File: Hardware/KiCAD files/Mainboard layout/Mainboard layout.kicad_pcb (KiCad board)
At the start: 2 copper layers, 125.7 x 122.4 mm, 62 parts, among them J1 Programmer pins Conn_01x02, J10 Conn_01x02, J11 Conn_01x06, J12 JST_06, J13 Conn_01x08, J14 Conn_01x03, J15 Conn_01x03, J17 Conn_01x06, J19 Conn_01x06, J2 Screw_Terminal_2_P5.00mm, J21 Conn_01x06, J22 Conn_01x03, J23 Conn_01x06, J24 Conn_01x06, J25 Conn_01x06, J26 Conn_01x06, J28 Conn_01x03, J29 Conn_01x03, J3 Screw_Terminal_2_P3.50mm, J30 USB-A1VSB6, J31 JST_03, J34 JST_03, J35 JST_03, J36 JST_03, J37 JST_03, J38 JST_03, J4 JST_06, J5 Conn_01x04, J6 JST_06, J7 JST_06, J8 Conn_01x06, J9 Conn_01x10, Q2 2DD1664, Q5 2N7000, SW8 Push_Button, SW9 Push_Button, U12 ESP32-S3-WROOM-1, U3 PCA9534PW, U5 PCA9534PW

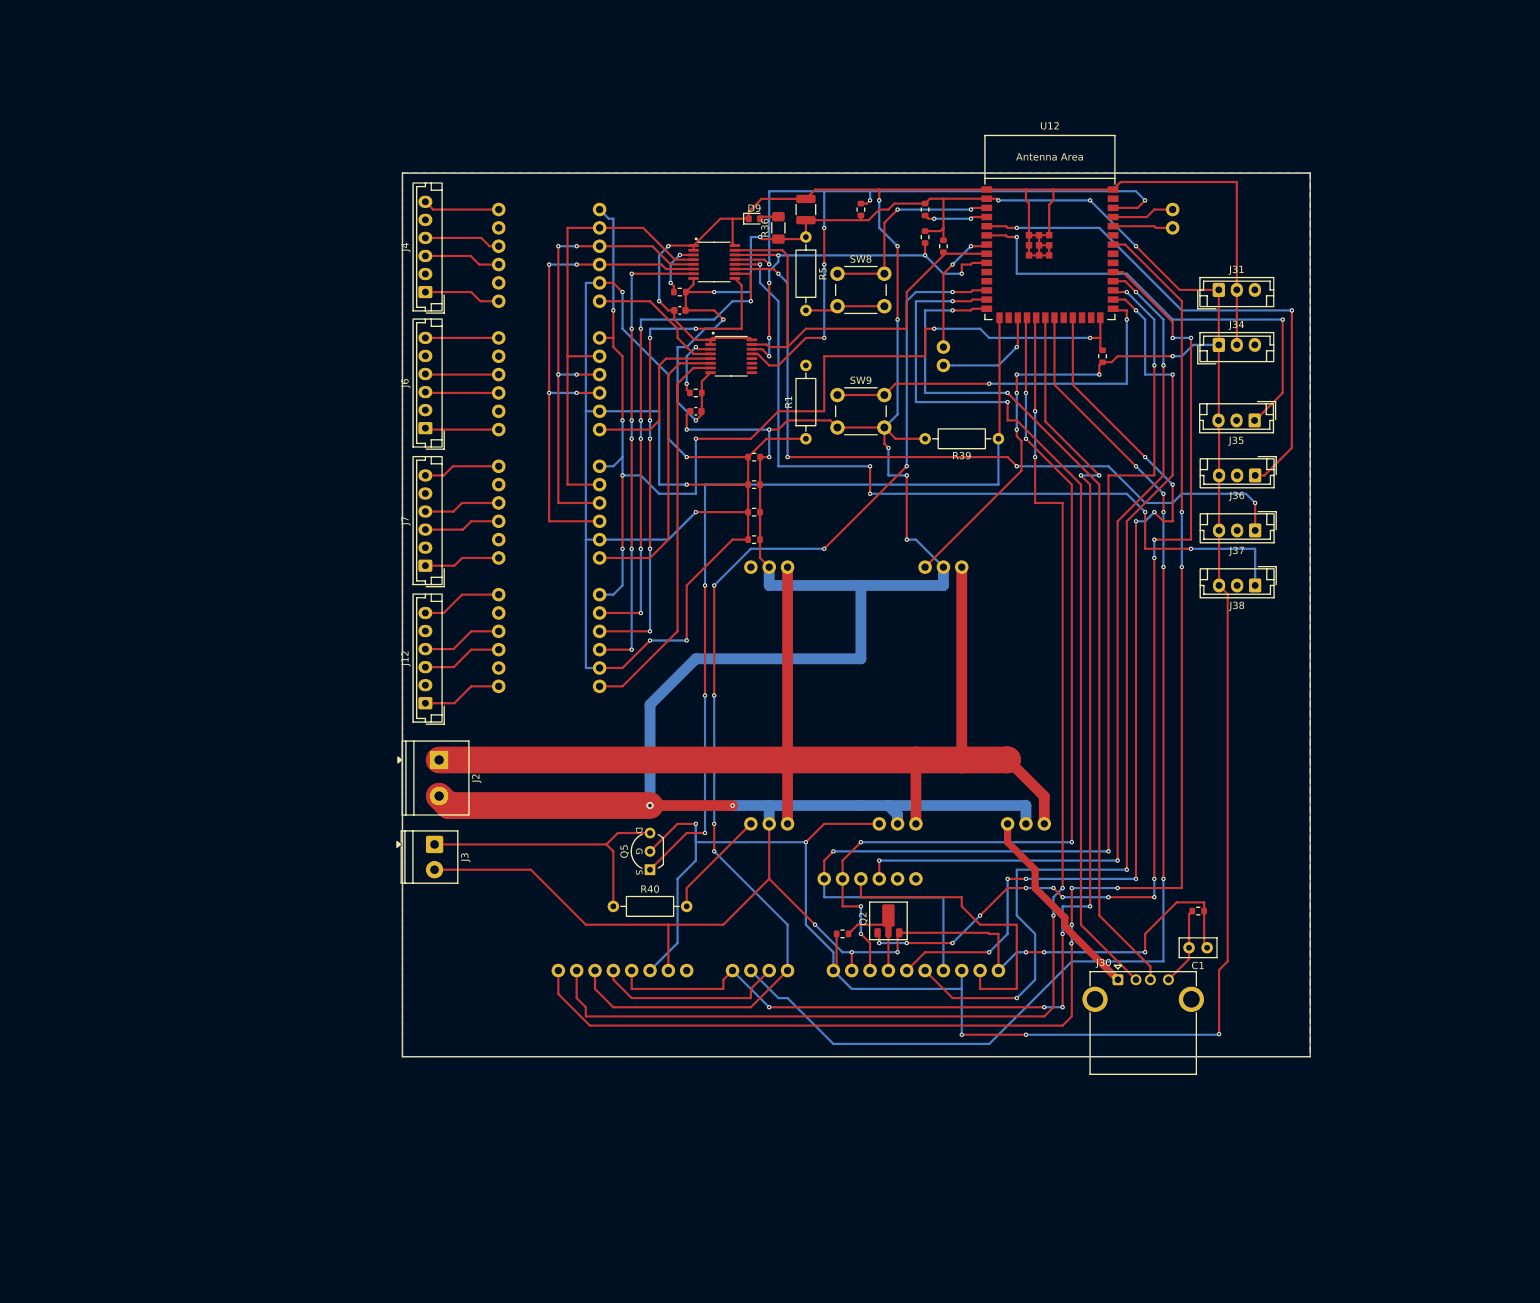
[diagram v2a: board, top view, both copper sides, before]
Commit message: 1st push of PCB's for printing
This is pre-peer review. This almost certainly has section that need adjustment. also realized I'm missing the USB-Uart bridge. first thing added in next version.
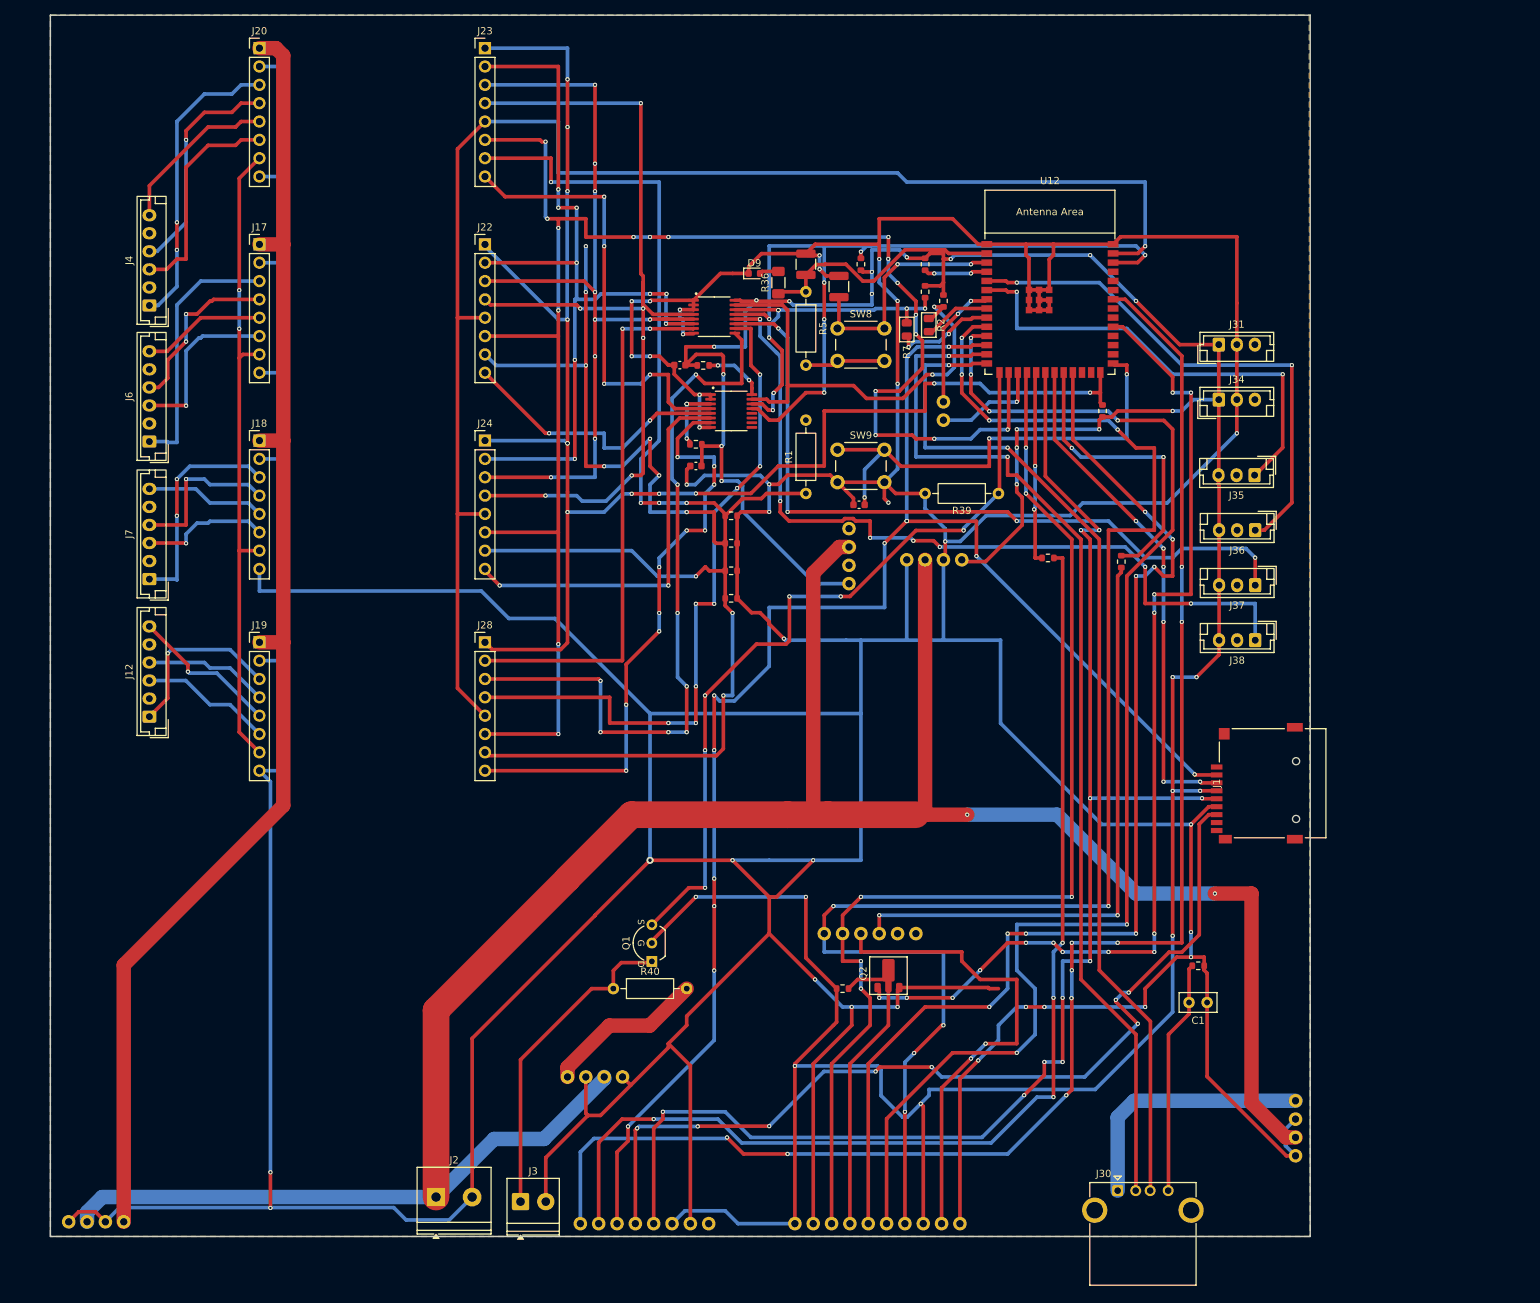
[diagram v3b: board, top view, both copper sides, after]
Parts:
- removed J14, J15, J29: Conn_01x03, PCM_SparkFun-Connector:1x03_P2.54mm
- removed J21: Conn_01x06, PCM_SparkFun-Connector:1x06_P2.54mm
- removed Q5: 2N7000, PCM_Package_TO_SOT_THT_AKL:TO-92_Inline_Wide_SGD
- removed R51: 10k, PCM_SparkFun-Resistor:R_0603_1608Metric
- added C3: 0.1uF, PCM_SparkFun-Capacitor:C_0603_1608Metric, F.Cu at (147.1, 59.9)
- added C4: 10uF, PCM_SparkFun-Capacitor:C_1210_3225Metric, F.Cu at (144.3, 29.7)
- added J18: PINHD_1x8_Male, Connector_PinHeader_2.54mm:PinHeader_1x08_P2.54mm_Vertical, F.Cu at (64.0, 51.1)
- added J20: PINHD_1x8_Male, Connector_PinHeader_2.54mm:PinHeader_1x08_P2.54mm_Vertical, F.Cu at (64.0, -3.30)
- added J27: Conn_01x04, PCM_SparkFun-Connector:1x04_P2.54mm, F.Cu at (106.7, 139.2)
- added Q1: BS170, PCM_Package_TO_SOT_THT_AKL:TO-92_Inline_Wide_DGS, F.Cu at (118.4, 123.2)
- added R2: 50 ohmR_0805, PCM_Resistor_SMD_AKL:R_0805_2012Metric, F.Cu at (156.7, 35.1)
- added R3: 100, PCM_SparkFun-Resistor:R_0603_1608Metric, F.Cu at (183.4, 67.8)
- added R4: 100, PCM_SparkFun-Resistor:R_0603_1608Metric, F.Cu at (173.2, 67.3)
- added R56: 10k, PCM_SparkFun-Resistor:R_0603_1608Metric, F.Cu at (124.5, 51.6)
- added R7: 50 ohm R_0805, PCM_Resistor_SMD_AKL:R_0805_2012Metric, F.Cu at (153.7, 35.7)
- J1: value Programmer pins Conn_01x02 -> MSD-1-A; footprint PCM_SparkFun-Connector:1x02_P2.54mm -> MMC_Footprints:CONN9_MSD-1_CUD
- J11, J25, J26: value Conn_01x06 -> Conn_01x04; footprint PCM_SparkFun-Connector:1x06_P2.54mm -> PCM_SparkFun-Connector:1x04_P2.54mm
- J17, J19, J23, J24: value Conn_01x06 -> PINHD_1x8_Male; footprint PCM_SparkFun-Connector:1x06_P2.54mm -> Connector_PinHeader_2.54mm:PinHeader_1x08_P2.54mm_Vertical
- J22, J28: value Conn_01x03 -> PINHD_1x8_Male; footprint PCM_SparkFun-Connector:1x03_P2.54mm -> Connector_PinHeader_2.54mm:PinHeader_1x08_P2.54mm_Vertical
- R50: value 10k -> 1k
- moved J11 137.7 mm to (45.2, 159.3), turned to 180 degrees
- moved J25 122.2 mm to (207.5, 142.5), turned to -90 degrees
- moved J1 80.7 mm to (204.3, 98.5), turned to 90 degrees
- moved J28 76.6 mm to (95.2, 79.0)
- moved J22 75.6 mm to (95.2, 23.9)
- moved J5 61.8 mm to (161.3, 67.6)
- moved J2 60.5 mm to (88.5, 155.8), turned to 0 degrees
- moved J3 50.9 mm to (100.2, 156.5), turned to 0 degrees
- moved J17 41.9 mm to (64.0, 23.9), turned to 0 degrees
- moved J23 38.5 mm to (95.2, -3.30), turned to 0 degrees
- moved J12 38.3 mm to (48.8, 89.3)
- moved J4 38.3 mm to (48.8, 32.3)
- moved J6 38.3 mm to (48.8, 51.2)
- moved J7 38.3 mm to (48.8, 70.2)
- moved J26 37.4 mm to (145.7, 70.9)
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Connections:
- J1 pad 1: /TX -> unconnected-(J1-DAT2-Pad1)
- J1 pad 2: /RX -> SPI1_CS
- J11 pad 1: B2_DRV0 -> +12V
- J11 pad 2: unconnected-(J11-Pin_2-Pad2) -> GND
- J11 pad 3: A2_DRV0 -> +24V
- J11 pad 4: B1_DRV0 -> GND
- J12 pad 1: B2_DRV3 -> B2_DRVE
- J12 pad 3: A2_DRV3 -> A2_DRVE
- J12 pad 4: B1_DRV3 -> B1_DRVE
- J12 pad 6: A1_DRV3 -> A1_DRVE
- J17 pad 1: B2_DRV1 -> +12V
- J17 pad 2: unconnected-(J17-Pin_2-Pad2) -> GND
- J17 pad 3: A2_DRV1 -> B2_DRV1
- J17 pad 5: unconnected-(J17-Pin_5-Pad5) -> A1_DRV1
- J17 pad 6: A1_DRV1 -> A2_DRV1
- J19 pad 1: B2_DRV2 -> +12V
- J19 pad 2: unconnected-(J19-Pin_2-Pad2) -> GND
- J19 pad 3: A2_DRV2 -> B2_DRVE
- J19 pad 4: B1_DRV2 -> B1_DRVE
- J19 pad 5: unconnected-(J19-Pin_5-Pad5) -> A1_DRVE
- J19 pad 6: A1_DRV2 -> A2_DRVE
- J22 pad 1: +3.3V -> N_ENBL
- J22 pad 2: GND -> MODE_2_GPIO
- J22 pad 3: +24V -> MODE_1_GPIO
- J23 pad 1: DIR0 -> N_ENBL
- J23 pad 2: DRIVER_0_STEP -> MODE_2_GPIO
- J23 pad 3: MODE_2_GPIO -> MODE_1_GPIO
- J23 pad 4: MODE_1_GPIO -> MODE_0_GPIO
- J23 pad 5: MODE_0_GPIO -> Reset
- J23 pad 6: N_ENBL -> nSLP
- J24 pad 1: DIR1 -> N_ENBL
- J24 pad 2: DRIVER_0_STEP -> MODE_2_GPIO
- J24 pad 3: MODE_2_GPIO -> MODE_1_GPIO
- J24 pad 4: MODE_1_GPIO -> MODE_0_GPIO
- J24 pad 5: MODE_0_GPIO -> Reset
- J24 pad 6: N_ENBL -> nSLP
- J25 pad 1: DIR2 -> +5V_HIGHPW
- J25 pad 2: DRIVER_0_STEP -> GND
- J25 pad 3: MODE_2_GPIO -> +24V
- J25 pad 4: MODE_1_GPIO -> GND
- J26 pad 1: DIR3 -> +3.3V
- J26 pad 2: DRIVER_0_STEP -> GND
- J26 pad 3: MODE_2_GPIOE -> +24V
- J26 pad 4: MODE_1_GPIOE -> GND
- J28 pad 1: +5V_HIGHPW -> N_ENBL
- J28 pad 2: GND -> MODE_2_GPIOE
- J28 pad 3: +24V -> MODE_1_GPIOE
- J5 pad 1: SPI1_CS -> +3.3V
- J5 pad 2: CHAINL0_MISO_1 -> GND
- J5 pad 3: MOSI_1 -> +24V
- J5 pad 4: SPI1_CLK -> GND
- R52 pad 1: Net-(U12-GPIO16/U0CTS/ADC2_CH5/XTAL_32K_N) -> Net-(U3-SCL)
- R53 pad 1: Net-(U12-GPIO15/U0RTS/ADC2_CH4/XTAL_32K_P) -> Net-(U3-SDA)
- R54 pad 1: +3.3V -> Net-(U5-VDD)
- R54 pad 2: Net-(U5-A2) -> +3.3V
- U12 pad 10: unconnected-(U12-GPIO17/U1TXD/ADC2_CH6-Pad10) -> SPI4_CLK
- U12 pad 11: unconnected-(U12-GPIO18/U1RXD/ADC2_CH7/CLK_OUT3-Pad11) -> MOSI_4
- U12 pad 16: unconnected-(U12-GPIO46-Pad16) -> nSLP
- U12 pad 19: MISO_1 -> Net-(U12-GPIO11/TOUCH11/ADC2_CH0/FSPID/FSPIIO5/SUBSPID)
- U12 pad 22: unconnected-(U12-GPIO14/TOUCH14/ADC2_CH3/FSPIWP/FSPIDQS/SUBSPIWP-Pad22) -> Net-(U12-GPIO14/TOUCH14/ADC2_CH3/FSPIWP/FSPIDQS/SUBSPIWP)
- U12 pad 28: MOSI_4 -> unconnected-(U12-SPIIO6/GPIO35/FSPID/SUBSPID-Pad28)
- U12 pad 29: SPI4_CLK -> unconnected-(U12-SPIIO7/GPIO36/FSPICLK/SUBSPICLK-Pad29)
- U12 pad 30: MISO_4 -> unconnected-(U12-SPIDQS/GPIO37/FSPIQ/SUBSPIQ-Pad30)
- U12 pad 39: unconnected-(U12-GPIO1/TOUCH1/ADC1_CH0-Pad39) -> Reset
- U3 pad 14: Net-(U12-GPIO16/U0CTS/ADC2_CH5/XTAL_32K_N) -> Net-(U3-SCL)
- U3 pad 15: Net-(U12-GPIO15/U0RTS/ADC2_CH4/XTAL_32K_P) -> Net-(U3-SDA)
- U3 pad 16: GND -> +3.3V
- U3 pad 3: Net-(U3-A2) -> GND
- U3 pad 8: +3.3V -> GND
- U5 pad 14: Net-(U12-GPIO16/U0CTS/ADC2_CH5/XTAL_32K_N) -> Net-(U3-SCL)
- U5 pad 15: Net-(U12-GPIO15/U0RTS/ADC2_CH4/XTAL_32K_P) -> Net-(U3-SDA)
- U5 pad 16: GND -> Net-(U5-VDD)
- U5 pad 7: DIR3 -> DIRE
- U5 pad 8: +3.3V -> GND
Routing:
- net GND: track 607.6 -> 1227.7 mm, vias 19 -> 35
- net nSLP: track 0.00 -> 231.9 mm, vias 0 -> 18
- net Reset: track 0.00 -> 205.9 mm, vias 0 -> 1
- net +24V: track 160.9 -> 347.8 mm, vias 0 -> 2
- net +12V: track 0.00 -> 184.3 mm
- net CHAINL0_MISO_1: track 26.2 -> 127.9 mm, vias 0 -> 8
- net MOSI_1: track 161.5 -> 70.4 mm, vias 5 -> 6
- net nFault: track 0.00 -> 90.4 mm, vias 0 -> 2
- net DIRE: track 0.00 -> 82.7 mm, vias 0 -> 10
- net +3.3V: track 452.2 -> 530.3 mm, vias 17 -> 26
- net DRIVER_0_STEP: track 205.5 -> 282.4 mm, vias 6 -> 14
- net N_ENBL: track 156.1 -> 226.6 mm, vias 7 -> 12
- net MODE_0_GPIO: track 63.7 -> 129.8 mm, vias 0 -> 6
- net Net-(U3-SDA): track 0.00 -> 64.1 mm, vias 0 -> 2
- net SPI1_CS: track 158.0 -> 220.8 mm, vias 7 -> 12
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- added copper zone on B.Cu, net GND
- added copper zone on F.Cu, net GND
- removed copper zone on F.Cu, net (none)
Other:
- board size 125.7 x 122.4 mm -> 174.5 x 169.2 mm
